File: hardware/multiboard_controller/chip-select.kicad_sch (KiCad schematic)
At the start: 12 parts, among them SW1 OS102011MS2QN1, SW2 OS102011MS2QN1, SW3 OS102011MS2QN1, SW4 SW_SPST

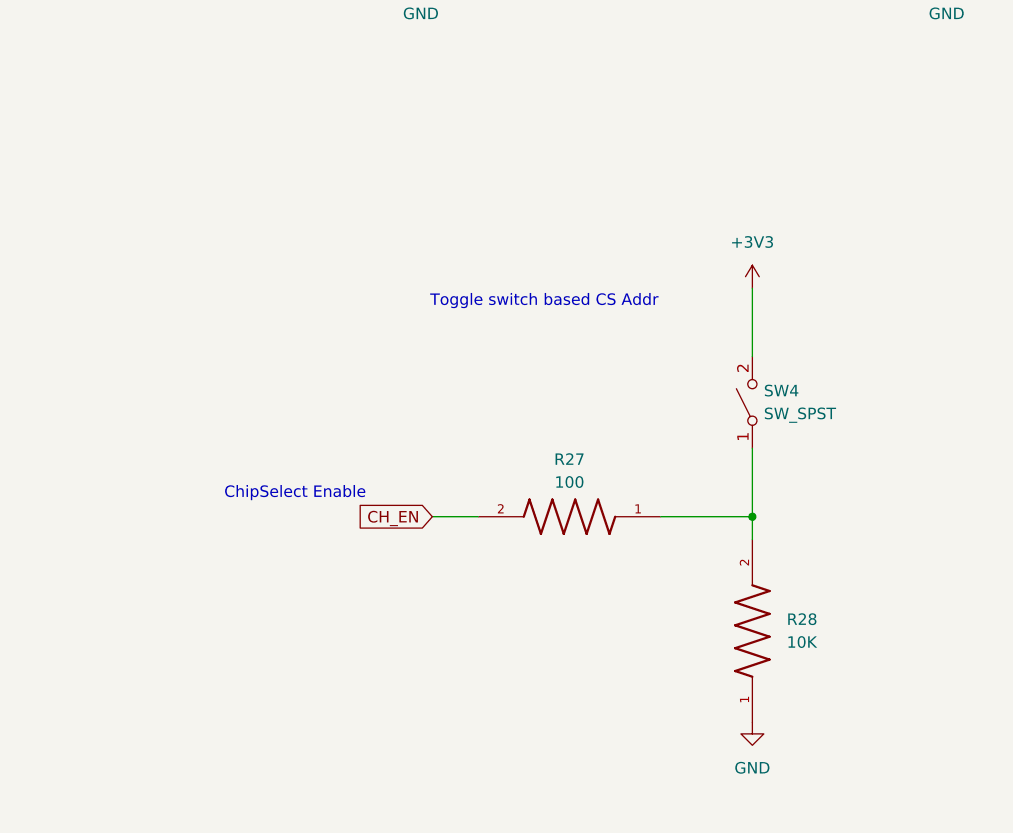
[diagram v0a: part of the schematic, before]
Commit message: Full USB-to-UART connections
- Connect switches and convertor IC in USB-UART mode
- Change CH_EN input signal from momentary button to switch to work with
  switch chips (since it expects high enable to output signal)

TODOs:
- Confirm that resistors built into ICs are enough to protect USB/UART
  signals.
- Rework select circuitry to automatically enable after certain time
  period (but without adding ucontroller) -- possibly using caps or 555?
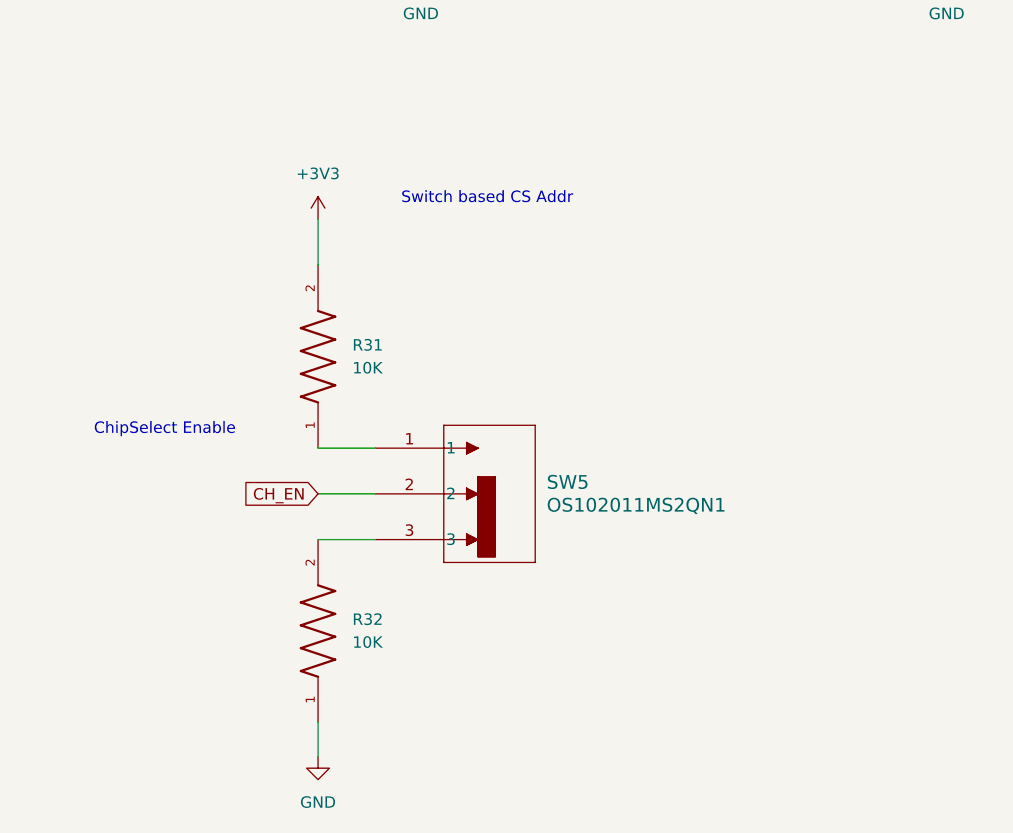
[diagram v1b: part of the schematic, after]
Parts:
- removed R27: 100, symbol ERJ2RKF1002X:ERJ2RKF1002X
- removed R28: 10K, ERJ2RKF1002X:RES_ERJ2RKF1002X, symbol ERJ2RKF1002X:ERJ2RKF1002X
- removed SW4: SW_SPST, symbol Switch:SW_SPST
- added R31, R32: 10K, ERJ2RKF1002X:RES_ERJ2RKF1002X, symbol ERJ2RKF1002X:ERJ2RKF1002X
- added SW5: OS102011MS2QN1, SPDT_OS102011_CNK, symbol 2025-02-13_02-16-07:OS102011MS2QN1
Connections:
- net +3V3: now also R31.2
- net CH_EN: now also SW5.2
- net GND: now also R32.1
- new net: R31.1, SW5.1
- new net: R32.2, SW5.3
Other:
- note added: "Switch based CS Addr"
- note removed: "Toggle switch based CS Addr"

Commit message: Starting layout
Add serial ground connections, add footprint libraries, start layout.
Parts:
- R21, R22, R23, R24, R25, R26, R31, R32: footprint ERJ2RKF1002X:RES_ERJ2RKF1002X -> all-footprints:RES_ERJ2RKF1002X
- renumbered SW3 to SW0
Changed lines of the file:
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@@
 			)
 		)
-		(property "Description" ""
+		(property "Description" "Power symbol creates a global label with name \"GND\" , ground"
 			(at 48.26 180.34 0)
 			(effects
@@
 			)
 		)
-		(property "Description" ""
+		(property "Description" "Power symbol creates a global label with name \"GND\" , ground"
 			(at 59.69 92.71 0)
 			(effects
@@
 			)
 		)
-		(property "Footprint" "ERJ2RKF1002X:RES_ERJ2RKF1002X"
+		(property "Footprint" "all-footprints:RES_ERJ2RKF1002X"
 			(at 59.69 48.26 0)
 			(effects
@@
 		(dnp no)
 		(fields_autoplaced yes)
-		(property "Reference" "SW3"
+		(property "Reference" "SW0"
 			(at 201.93 60.9599 0)
 			(effects
@@
 			(project "multiboard_controller"
 				(path "/0fe19ce7-810a-40c6-903d-4212edc122f9/e301144b-e109-475e-9cb5-ffd4ffbe7b79"
-					(reference "SW3")
+					(reference "SW0")
 					(unit 1)
 				)
@@
 			)
 		)
-		(property "Footprint" "ERJ2RKF1002X:RES_ERJ2RKF1002X"
+		(property "Footprint" "all-footprints:RES_ERJ2RKF1002X"
 			(at 48.26 135.89 0)
 			(effects
@@
 			)
 		)
-		(property "Description" ""
+		(property "Description" "Power symbol creates a global label with name \"+3V3\""
 			(at 59.69 33.02 0)
 			(effects
@@
 			)
 		)
-		(property "Footprint" "ERJ2RKF1002X:RES_ERJ2RKF1002X"
+		(property "Footprint" "all-footprints:RES_ERJ2RKF1002X"
 			(at 176.53 46.99 0)
 			(effects
@@
 			)
 		)
-		(property "Footprint" "ERJ2RKF1002X:RES_ERJ2RKF1002X"
+		(property "Footprint" "all-footprints:RES_ERJ2RKF1002X"
 			(at 48.26 166.37 0)
 			(effects
@@
 			)
 		)
-		(property "Description" ""
+		(property "Description" "Power symbol creates a global label with name \"GND\" , ground"
 			(at 176.53 91.44 0)
 			(effects
@@
 			)
 		)
-		(property "Description" ""
+		(property "Description" "Power symbol creates a global label with name \"+3V3\""
 			(at 48.26 120.65 0)
 			(effects
@@
 			)
 		)
-		(property "Footprint" "ERJ2RKF1002X:RES_ERJ2RKF1002X"
+		(property "Footprint" "all-footprints:RES_ERJ2RKF1002X"
 			(at 176.53 77.47 0)
 			(effects
@@
 			)
 		)
-		(property "Description" ""
+		(property "Description" "Power symbol creates a global label with name \"GND\" , ground"
 			(at 118.11 92.71 0)
 			(effects
@@
 			)
 		)
-		(property "Footprint" "ERJ2RKF1002X:RES_ERJ2RKF1002X"
+		(property "Footprint" "all-footprints:RES_ERJ2RKF1002X"
 			(at 118.11 48.26 0)
 			(effects
@@
 			)
 		)
-		(property "Footprint" "ERJ2RKF1002X:RES_ERJ2RKF1002X"
+		(property "Footprint" "all-footprints:RES_ERJ2RKF1002X"
 			(at 59.69 78.74 0)
 			(effects
@@
 			)
 		)
-		(property "Description" ""
+		(property "Description" "Power symbol creates a global label with name \"+3V3\""
 			(at 176.53 31.75 0)
 			(effects
@@
 			)
 		)
-		(property "Description" ""
+		(property "Description" "Power symbol creates a global label with name \"+3V3\""
 			(at 118.11 33.02 0)
 			(effects
@@
 			)
 		)
-		(property "Footprint" "ERJ2RKF1002X:RES_ERJ2RKF1002X"
+		(property "Footprint" "all-footprints:RES_ERJ2RKF1002X"
 			(at 118.11 78.74 0)
 			(effects
